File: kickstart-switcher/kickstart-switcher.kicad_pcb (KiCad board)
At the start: 2 copper layers, 20.3 x 31.1 mm, 13 parts, among them P1 CONN_01X04, Q1 Q_NMOS_GSD, U1 74HC74, U2 74HC14

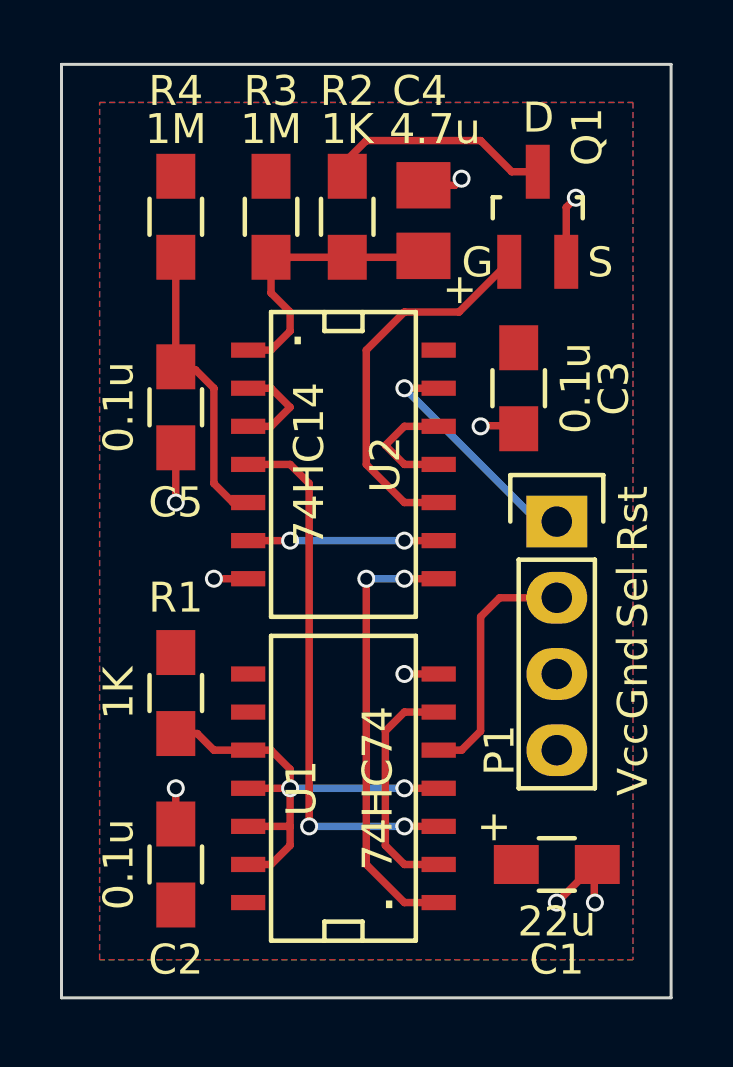
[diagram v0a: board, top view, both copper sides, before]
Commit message: kickstart-switcher: Add 1K protection resistors to RC delay HCMOS inputs. Prevents excessive current through over-voltage diodes on power down.
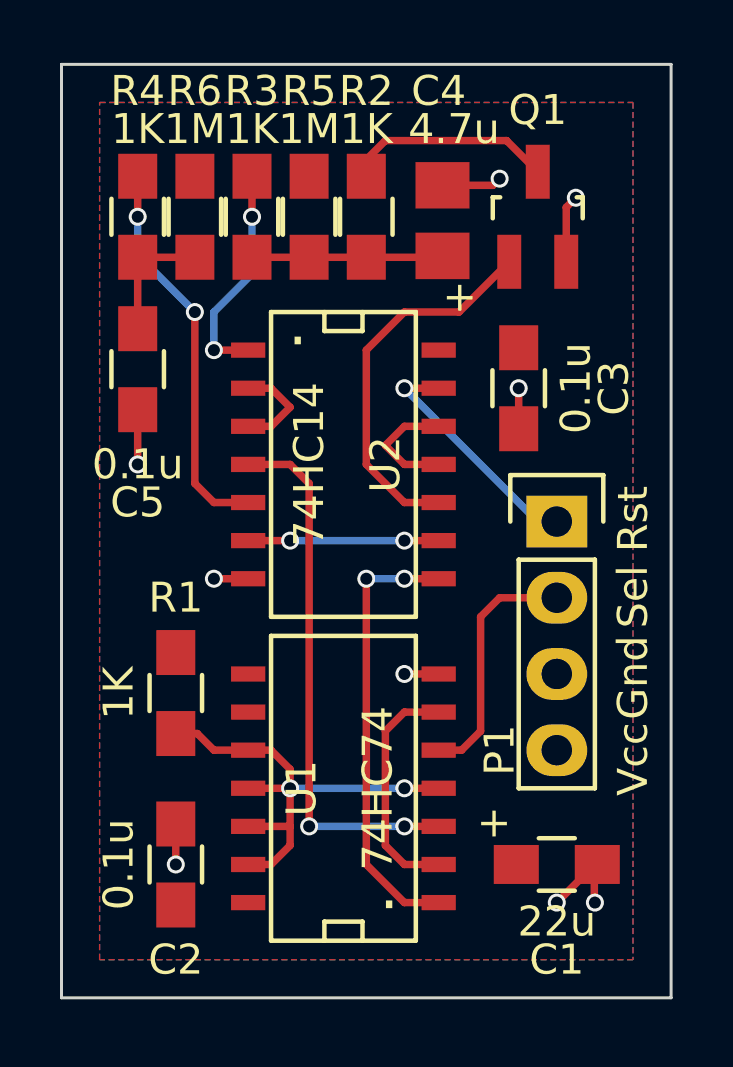
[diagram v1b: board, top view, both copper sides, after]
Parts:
- added R5: 1M, Resistors_SMD:R_0805_HandSoldering, F.Cu at (146.7, 96.5)
- added R6: 1M, Resistors_SMD:R_0805_HandSoldering, F.Cu at (142.9, 96.5)
- Q1: value Q_NMOS_GSD -> Q_NMOS
- R3, R4: value 1M -> 1K
- moved C5 1.80 mm to (141.0, 101.6)
- moved R4 1.27 mm to (141.0, 96.5)
- moved C4 0.63 mm to (151.1, 96.6)
- moved R2 0.63 mm to (148.6, 96.5)
- moved R3 0.63 mm to (144.8, 96.5)
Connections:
- R3 pad 1: VCC -> Net-(R3-Pad1)
- R4 pad 1: VCC -> Net-(R4-Pad1)
- U2 pad 1: Net-(C4-Pad1) -> Net-(R3-Pad1)
- U2 pad 5: Net-(C5-Pad1) -> Net-(R4-Pad1)
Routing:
- net Net-(R4-Pad1): track 0.00 -> 13.6 mm, vias 0 -> 2
- net Net-(R3-Pad1): track 0.00 -> 7.46 mm, vias 0 -> 2
- net Net-(C5-Pad1): track 9.86 -> 4.28 mm
- net Net-(C4-Pad1): track 9.79 -> 6.79 mm
- net GND: track 13.5 -> 14.2 mm
- net Net-(Q1-Pad3): track 7.60 -> 6.96 mm
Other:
- board text removed: "D"
- board text removed: "G"
- board text removed: "S"

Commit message: kickstart-switcher: Use second 74HC74 flip-flop to generate extra select line and allow 4-way image selection
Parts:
- P1: value CONN_01X04 -> CONN_01X05; footprint Pin_Headers:Pin_Header_Straight_1x04 -> Pin_Headers:Pin_Header_Straight_1x05
- moved C1 1.91 mm to (154.9, 120.0)
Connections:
- net /SELECT renamed /SEL0
- C1 pad 1: VCC -> +5V
- C2 pad 1: VCC -> +5V
- C3 pad 1: VCC -> +5V
- P1 pad 3: GND -> /SEL1
- P1 pad 4: VCC -> GND
- R1 pad 1: VCC -> +5V
- R1 pad 2: /P_UP -> Net-(R1-Pad2)
- R5 pad 1: VCC -> +5V
- R6 pad 1: VCC -> +5V
- U1 pad 1: Net-(U1-Pad1) -> /CLR
- U1 pad 10: /P_UP -> Net-(R1-Pad2)
- U1 pad 11: /P_UP -> Net-(U1-Pad11)
- U1 pad 12: /P_UP -> Net-(U1-Pad12)
- U1 pad 13: /P_UP -> /CLR
- U1 pad 14: VCC -> +5V
- U1 pad 2: Net-(U1-Pad2) -> Net-(U1-Pad11)
- U1 pad 4: /P_UP -> Net-(R1-Pad2)
- U1 pad 6: Net-(U1-Pad2) -> Net-(U1-Pad11)
- U1 pad 8: Net-(U1-Pad8) -> Net-(U1-Pad12)
- U1 pad 9: Net-(U1-Pad9) -> /SEL1
- U2 pad 14: VCC -> +5V
- U2 pad 8: Net-(U1-Pad1) -> /CLR
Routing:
- net /CLR: track 0.00 -> 18.8 mm, vias 0 -> 2
- net /P_UP: track 16.2 -> 0.00 mm, vias 2 -> 0
- net Net-(U1-Pad1): track 14.9 -> 0.00 mm, vias 2 -> 0
- net /SEL1: track 0.00 -> 14.8 mm, vias 0 -> 2
- net Net-(U1-Pad11): track 0.00 -> 12.5 mm, vias 0 -> 2
- net Net-(R1-Pad2): track 0.00 -> 9.89 mm, vias 0 -> 2
- net Net-(U1-Pad12): track 0.00 -> 8.40 mm
- net Net-(U1-Pad2): track 7.89 -> 0.00 mm
- added copper zone on F.Cu, net +5V
- removed copper zone on F.Cu, net VCC
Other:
- board text added: "4-Way Kickstart Switcher v2.0"
- board text added: "S0"
- board text added: "S1"
- board text added: "github.com/keirf/PCB-Projects"
- board text removed: "Sel"
